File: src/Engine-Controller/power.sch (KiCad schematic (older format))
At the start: 21 parts, among them J1 4840.2201, U2 LM22672MRE-5.0_NOPB, U3 LMS8117AMP-3.3_NOPB

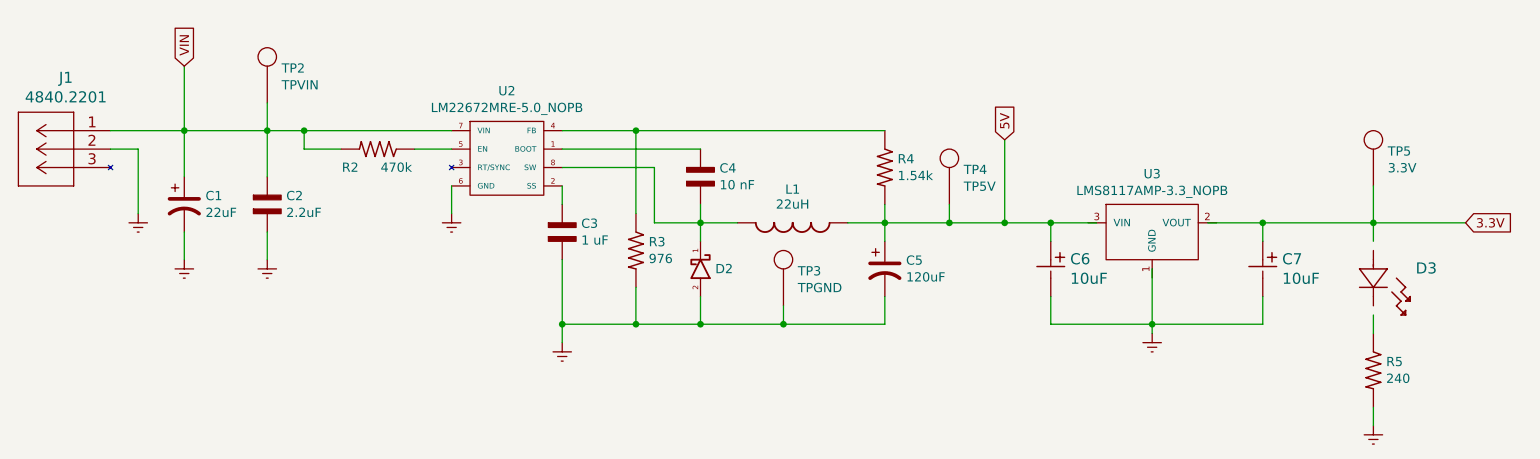
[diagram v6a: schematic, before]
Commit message: Updated Connector pinouts and added button to Reset pin
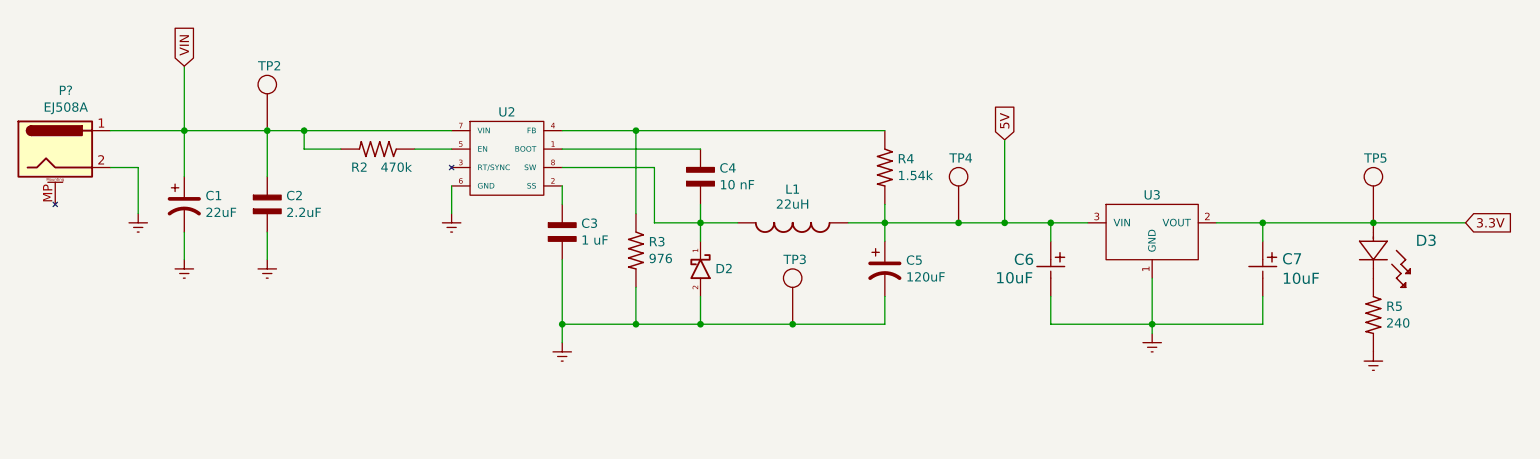
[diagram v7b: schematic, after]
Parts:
- removed J1: 4840.2201, Engine-Controller:12V_power_jack, symbol Engine-Controller:4840.2201
- added P?: EJ508A, symbol Engine-Controller:EJ508A
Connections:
- wire segments 61 -> 54
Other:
- moved on the sheet: D3, R5, TP2, TP3, TP4, TP5
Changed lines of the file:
@@
 L Engine-Controller:LTST-C150GKT D3
 U 1 1 60EB9E6E
-P 9300 4350
-F 0 "D3" H 9529 4453 60  0000 L CNN
-F 1 "LTST-C150GKT" H 9529 4347 60  0001 L CNN
-F 2 "Engine-Controller:LTST-C150GKT" H 9500 3990 60  0001 C CNN
-F 3 "" V 9300 4600 60  0000 C CNN
-	1    9300 4350
+P 9300 4200
+F 0 "D3" H 9529 4303 60  0000 L CNN
+F 1 "LTST-C150GKT" H 9529 4197 60  0001 L CNN
+F 2 "Engine-Controller:LTST-C150GKT" H 9500 3840 60  0001 C CNN
+F 3 "" V 9300 4450 60  0000 C CNN
+	1    9300 4200
 	1    0    0    -1
 $EndComp
@@
 U 1 1 60EBB9CF
 P 8100 4050
-F 0 "U3" H 8100 4365 50  0000 C CNN
-F 1 "LMS8117AMP-3.3_NOPB" H 8100 4274 50  0000 C CNN
+F 0 "U3" H 8100 4250 50  0000 C CNN
+F 1 "LMS8117AMP-3.3_NOPB" H 8100 4274 50  0001 C CNN
 F 2 "Engine-Controller:SOT-223" H 8100 4050 50  0001 C CNN
 F 3 "" H 8100 4050 50  0001 C CNN
@@
 $EndComp
 Wire Wire Line
-	2450 3600 2600 3600
-Wire Wire Line
-	2600 3600 2600 3950
+	2450 3700 2600 3700
 Text GLabel 2850 3150 1    50   Input ~ 0
 VIN
@@
 U 1 1 60EEF47A
 P 3900 3600
-F 0 "R2" H 4050 3700 50  0000 C CNN
+F 0 "R2" H 4000 3700 50  0000 C CNN
 F 1 "470k" H 3800 3700 50  0000 C CNN
 F 2 "Engine-Controller:RES_0805" H 3950 3100 50  0001 L BNN
@@
 Connection ~ 5650 4550
 Wire Wire Line
-	5650 4550 6100 4550
-Wire Wire Line
 	5300 3950 5300 3500
 Connection ~ 5300 3500
@@
 Wire Wire Line
 	5300 4550 5650 4550
-Wire Wire Line
-	7800 4000 7550 4000
 Text GLabel 7300 3550 1    50   Input ~ 0
 5V
 Wire Wire Line
 	7300 3550 7300 4000
-Connection ~ 7300 4000
-Wire Wire Line
-	7300 4000 7000 4000
 $Comp
 L power:Earth #PWR0108
@@
 Wire Wire Line
 	7550 4100 7550 4000
-Connection ~ 7550 4000
 Wire Wire Line
 	7550 4000 7300 4000
-Wire Wire Line
-	8100 4250 8100 4550
 Wire Wire Line
 	7550 4400 7550 4550
@@
 Wire Wire Line
 	8100 4550 8100 4600
-Wire Wire Line
-	8400 4000 8700 4000
 Wire Wire Line
 	8700 4000 8700 4100
@@
 Text GLabel 9800 4000 2    50   Input ~ 0
 3.3V
-Connection ~ 8700 4000
 Wire Wire Line
 	8700 4000 9300 4000
-Wire Wire Line
-	9300 4000 9300 4100
 Connection ~ 9300 4000
 Wire Wire Line
@@
 L Engine-Controller:RES_0603 R5
 U 1 1 60ED1BD1
-P 9300 4800
-F 0 "R5" V 9254 4869 50  0000 L CNN
-F 1 "240" V 9345 4869 50  0000 L CNN
-F 2 "Engine-Controller:RES_0603" H 9350 4300 50  0001 L BNN
-F 3 "" H 9300 4800 50  0001 L BNN
-	1    9300 4800
-	0    1    1    0
-$EndComp
-Wire Wire Line
-	9300 4500 9300 4600
+P 9300 4500
+F 0 "R5" V 9254 4569 50  0000 L CNN
+F 1 "240" V 9345 4569 50  0000 L CNN
+F 2 "Engine-Controller:RES_0603" H 9350 4000 50  0001 L BNN
+F 3 "" H 9300 4500 50  0001 L BNN
+	1    9300 4500
+	0    1    1    0
+$EndComp
 $Comp
 L power:Earth #PWR0109
 U 1 1 60ED92F3
-P 9300 5100
-F 0 "#PWR0109" H 9300 4850 50  0001 C CNN
-F 1 "Earth" H 9300 4950 50  0001 C CNN
-F 2 "" H 9300 5100 50  0001 C CNN
-F 3 "~" H 9300 5100 50  0001 C CNN
-	1    9300 5100
-	1    0    0    -1
-$EndComp
-Wire Wire Line
-	9300 5000 9300 5100
+P 9300 4700
+F 0 "#PWR0109" H 9300 4450 50  0001 C CNN
+F 1 "Earth" H 9300 4550 50  0001 C CNN
+F 2 "" H 9300 4700 50  0001 C CNN
+F 3 "~" H 9300 4700 50  0001 C CNN
+	1    9300 4700
+	1    0    0    -1
+$EndComp
 $Comp
 L Engine-Controller:LM22672MRE-5.0_NOPB U2
 U 1 1 611B83F2
 P 4600 3700
-F 0 "U2" H 4600 4115 50  0000 C CNN
-F 1 "LM22672MRE-5.0_NOPB" H 4600 4024 50  0000 C CNN
+F 0 "U2" H 4600 4000 50  0000 C CNN
+F 1 "LM22672MRE-5.0_NOPB" H 4600 4024 50  0001 C CNN
 F 2 "Engine-Controller:LM22672MRE-5.0_NOPB" H 4550 3700 50  0001 C CNN
 F 3 "" H 4550 3700 50  0001 C CNN
@@
 U 1 1 611C3D38
 P 7550 4100
-F 0 "C6" V 7647 4205 60  0000 L CNN
-F 1 "10uF" V 7753 4205 60  0000 L CNN
+F 0 "C6" V 7650 3900 60  0000 L CNN
+F 1 "10uF" V 7750 3800 60  0000 L CNN
 F 2 "Engine-Controller:CWR11HH106KB" H 7700 3740 60  0001 C CNN
 F 3 "" H 7550 4100 60  0000 C CNN
@@
 $EndComp
 $Comp
-L Engine-Controller:4840.2201 J1
-U 1 1 61252962
-P 2450 3500
-F 0 "J1" H 2692 3787 60  0000 C CNN
-F 1 "4840.2201" H 2692 3681 60  0000 C CNN
-F 2 "Engine-Controller:12V_power_jack" H 2850 2900 60  0001 C CNN
-F 3 "" H 2450 3500 60  0000 C CNN
-	1    2450 3500
-	-1   0    0    -1
-$EndComp
-$Comp
 L Engine-Controller:TP TP2
 U 1 1 60E67C30
-P 3300 3350
-F 0 "TP2" H 3378 3538 50  0000 L CNN
-F 1 "TPVIN" H 3378 3447 50  0000 L CNN
-F 2 "Engine-Controller:TP" H 3300 3350 50  0001 C CNN
-F 3 "" H 3300 3350 50  0001 C CNN
-	1    3300 3350
-	1    0    0    -1
-$EndComp
-Wire Wire Line
-	3300 3500 3300 3350
+P 3300 3500
+F 0 "TP2" H 3250 3850 50  0000 L CNN
+F 1 "TPVIN" H 3378 3597 50  0001 L CNN
+F 2 "Engine-Controller:TP" H 3300 3500 50  0001 C CNN
+F 3 "" H 3300 3500 50  0001 C CNN
+	1    3300 3500
+	1    0    0    -1
+$EndComp
+$Comp
+L Engine-Controller:TP TP3
+U 1 1 60E8595F
+P 6150 4550
+F 0 "TP3" H 6100 4900 50  0000 L CNN
+F 1 "TPGND" H 6228 4647 50  0001 L CNN
+F 2 "Engine-Controller:TP" H 6150 4550 50  0001 C CNN
+F 3 "" H 6150 4550 50  0001 C CNN
+	1    6150 4550
+	1    0    0    -1
+$EndComp
+$Comp
+L Engine-Controller:TP TP5
+U 1 1 60E93926
+P 9300 4000
+F 0 "TP5" H 9250 4350 50  0000 L CNN
+F 1 "3.3V" H 9378 4097 50  0001 L CNN
+F 2 "Engine-Controller:TP" H 9300 4000 50  0001 C CNN
+F 3 "" H 9300 4000 50  0001 C CNN
+	1    9300 4000
+	1    0    0    -1
+$EndComp
+$Comp
+L Engine-Controller:EJ508A P?
+U 1 1 60E212B8
+P 2150 3600
+F 0 "P?" H 2207 3917 50  0000 C CNN
+F 1 "EJ508A" H 2207 3826 50  0000 C CNN
+F 2 "" H 2200 3560 50  0001 C CNN
+F 3 "~" H 2200 3560 50  0001 C CNN
+	1    2150 3600
+	1    0    0    -1
+$EndComp
+Wire Wire Line
+	2600 3700 2600 3950
+Wire Wire Line
+	6650 4000 7050 4000
+Connection ~ 7300 4000
+Connection ~ 7050 4000
+Wire Wire Line
+	7050 4000 7300 4000
 $Comp
 L Engine-Controller:TP TP4
 U 1 1 60E7A9D7
-P 7000 3900
-F 0 "TP4" H 7078 4088 50  0000 L CNN
-F 1 "TP5V" H 7078 3997 50  0000 L CNN
-F 2 "Engine-Controller:TP" H 7000 3900 50  0001 C CNN
-F 3 "" H 7000 3900 50  0001 C CNN
-	1    7000 3900
-	1    0    0    -1
-$EndComp
-Wire Wire Line
-	7000 4000 7000 3900
-Connection ~ 7000 4000
-Wire Wire Line
-	7000 4000 6650 4000
-$Comp
-L Engine-Controller:TP TP3
-U 1 1 60E8595F
-P 6100 4450
-F 0 "TP3" H 6178 4638 50  0000 L CNN
-F 1 "TPGND" H 6178 4547 50  0000 L CNN
-F 2 "Engine-Controller:TP" H 6100 4450 50  0001 C CNN
-F 3 "" H 6100 4450 50  0001 C CNN
-	1    6100 4450
-	1    0    0    -1
-$EndComp
-Wire Wire Line
-	6100 4550 6100 4450
-Connection ~ 6100 4550
-Wire Wire Line
-	6100 4550 6650 4550
-$Comp
-L Engine-Controller:TP TP5
-U 1 1 60E93926
-P 9300 3800
-F 0 "TP5" H 9378 3988 50  0000 L CNN
-F 1 "3.3V" H 9378 3897 50  0000 L CNN
-F 2 "Engine-Controller:TP" H 9300 3800 50  0001 C CNN
-F 3 "" H 9300 3800 50  0001 C CNN
-	1    9300 3800
-	1    0    0    -1
-$EndComp
-Wire Wire Line
-	9300 3800 9300 4000
+P 7050 4000
+F 0 "TP4" H 7000 4350 50  0000 L CNN
+F 1 "TP5V" H 7128 4097 50  0001 L CNN
+F 2 "Engine-Controller:TP" H 7050 4000 50  0001 C CNN
+F 3 "" H 7050 4000 50  0001 C CNN
+	1    7050 4000
+	1    0    0    -1
+$EndComp
+Wire Wire Line
+	5650 4550 6150 4550
+Connection ~ 6150 4550
+Wire Wire Line
+	6150 4550 6650 4550
+Wire Wire Line
+	7750 4000 7550 4000
+Connection ~ 7550 4000
+Wire Wire Line
+	8450 4000 8700 4000
+Connection ~ 8700 4000
+Wire Wire Line
+	8100 4550 8100 4300
 $EndSCHEMATC

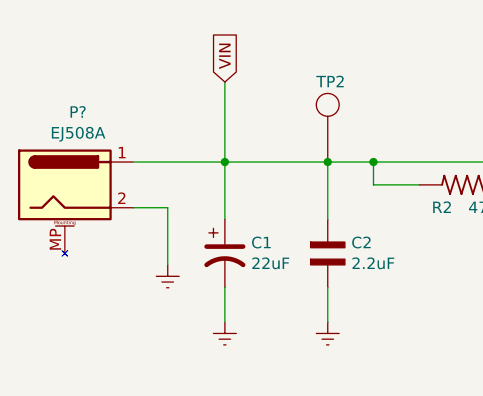
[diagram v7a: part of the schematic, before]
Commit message: Added buffer to some IOs
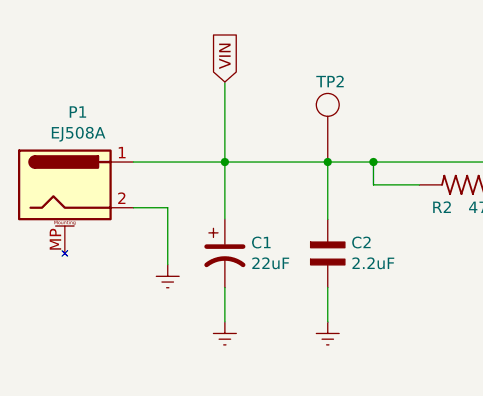
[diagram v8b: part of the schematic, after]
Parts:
- gave numbers to parts that had none: 1
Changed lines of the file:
@@
 $EndComp
 $Comp
-L Engine-Controller:EJ508A P?
+L Engine-Controller:EJ508A P1
 U 1 1 60E212B8
 P 2150 3600
-F 0 "P?" H 2207 3917 50  0000 C CNN
+F 0 "P1" H 2207 3917 50  0000 C CNN
 F 1 "EJ508A" H 2207 3826 50  0000 C CNN
 F 2 "" H 2200 3560 50  0001 C CNN
